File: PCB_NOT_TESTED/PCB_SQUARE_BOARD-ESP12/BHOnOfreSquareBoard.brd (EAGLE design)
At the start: 47.5 x 47.6 mm, 23 parts, among them J6 8p, J7 8p, K1 OMRON-G3MB-202P-SSR2, K2 OMRON-G3MB-202P-SSR2, Q1 S8050, U2 esp12, X2 PLUG

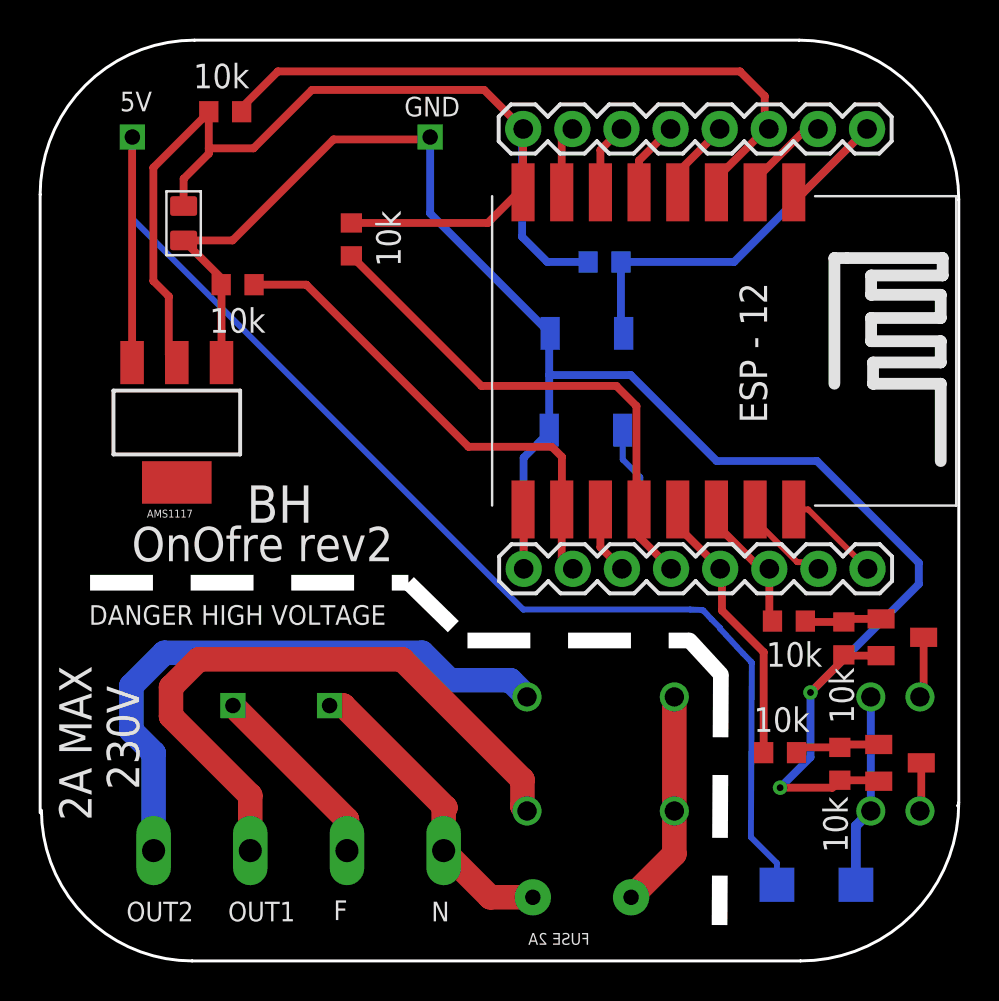
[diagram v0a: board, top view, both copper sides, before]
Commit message: change switch place
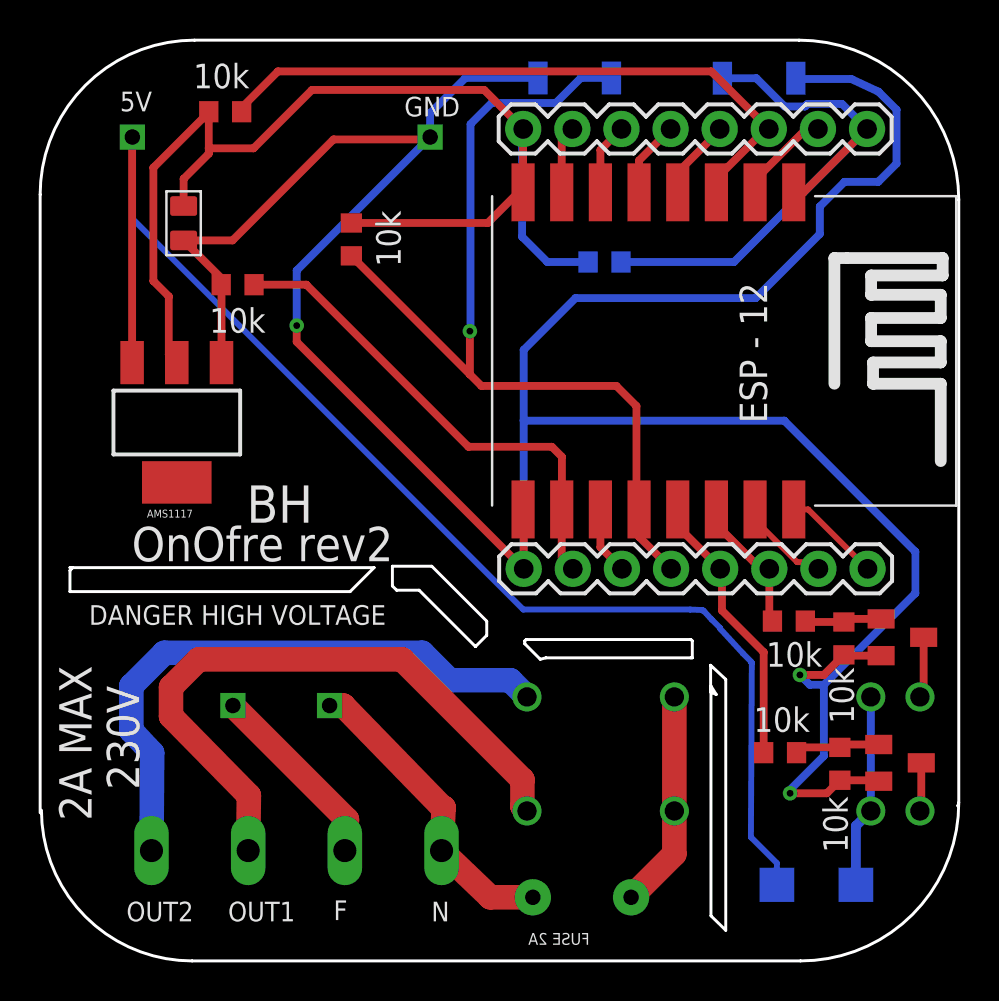
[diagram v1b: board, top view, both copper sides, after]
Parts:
- moved FLASH 18.2 mm to (27.8, 45.7)
- moved RESET 15.9 mm to (37.3, 45.6), turned to 180 degrees
- moved X2 0.11 mm to (13.4, 6.98)
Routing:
- net GND: track 98.4 -> 156.2 mm, vias 2 -> 3
- net GPIO0: track 35.7 -> 48.8 mm, vias 0 -> 1
- net RESET: track 24.5 -> 29.4 mm
- net CH_PD: track 34.8 -> 34.0 mm
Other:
- outline, holes or cut-outs redrawn
